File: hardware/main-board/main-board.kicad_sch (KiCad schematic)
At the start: 97 parts, among them J1 BOOT, J10 8P8CDouble, J11 Qwiic, J12 Qwiic, J13 Qwiic, J14 Micro_SD_Card_Det, J15 Interrupts1, J16 Interrupts2, J2 USB Header, J3 JTAG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

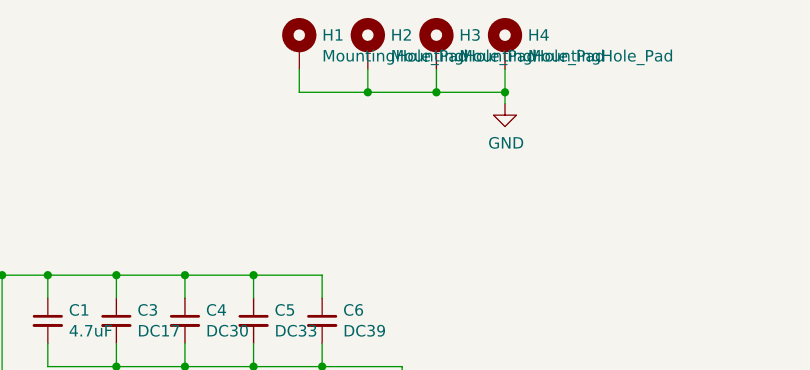
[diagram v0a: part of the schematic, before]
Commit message: Convert all other mounting holes to non-pad variety.
Reroute a few traces to be shorter.
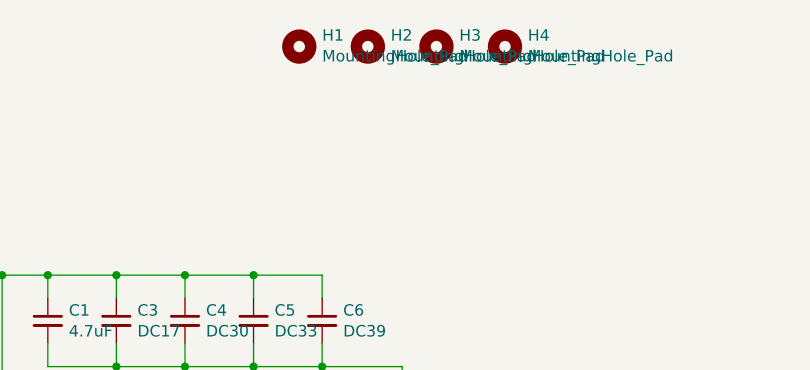
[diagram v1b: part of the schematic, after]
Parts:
- H1, H2, H3, H4: footprint Mounting_Holes:MountingHole_3.2mm_M3_Pad_Via -> MountingHole:MountingHole_3.2mm_M3; symbol Mechanical:MountingHole_Pad -> Mechanical:MountingHole
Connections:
- net GND: no longer H1.1, H2.1, H3.1, H4.1
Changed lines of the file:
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@@
   (junction (at 370.84 76.2) (diameter 0) (color 0 0 0 0)
   )
-  (junction (at 406.4 31.75) (diameter 0) (color 0 0 0 0)
-  )
   (junction (at 425.45 186.69) (diameter 0) (color 0 0 0 0)
   )
@@
   (junction (at 186.69 99.06) (diameter 0) (color 0 0 0 0)
   )
-  (junction (at 414.02 31.75) (diameter 0) (color 0 0 0 0)
-  )
   (junction (at 181.61 317.5) (diameter 0) (color 0 0 0 0)
   )
@@
   (junction (at 49.53 365.76) (diameter 0) (color 0 0 0 0)
   )
-  (junction (at 421.64 31.75) (diameter 0) (color 0 0 0 0)
-  )
   (no_connect (at 334.01 86.36))
   (no_connect (at 270.51 160.02))
@@
     (stroke (width 0) (type default) (color 0 0 0 0))
   )
-  (wire (pts (xy 414.02 29.21) (xy 414.02 31.75))
-    (stroke (width 0) (type default) (color 0 0 0 0))
-  )
   (wire (pts (xy 237.49 121.92) (xy 237.49 123.19))
     (stroke (width 0) (type default) (color 0 0 0 0))
@@
     (stroke (width 0) (type default) (color 0 0 0 0))
   )
-  (wire (pts (xy 421.64 31.75) (xy 421.64 29.21))
-    (stroke (width 0) (type default) (color 0 0 0 0))
-  )
   (wire (pts (xy 361.95 95.25) (xy 361.95 92.71))
     (stroke (width 0) (type default) (color 0 0 0 0))
@@
     (stroke (width 0) (type default) (color 0 0 0 0))
   )
-  (wire (pts (xy 398.78 31.75) (xy 406.4 31.75))
-    (stroke (width 0) (type default) (color 0 0 0 0))
-  )
   (wire (pts (xy 52.07 295.91) (xy 40.64 295.91))
     (stroke (width 0) (type default) (color 0 0 0 0))
@@
     (stroke (width 0) (type default) (color 0 0 0 0))
   )
-  (wire (pts (xy 421.64 33.02) (xy 421.64 31.75))
-    (stroke (width 0) (type default) (color 0 0 0 0))
-  )
   (wire (pts (xy 288.29 359.41) (xy 293.37 359.41))
     (stroke (width 0) (type default) (color 0 0 0 0))
@@
     (stroke (width 0) (type default) (color 0 0 0 0))
   )
-  (wire (pts (xy 406.4 29.21) (xy 406.4 31.75))
-    (stroke (width 0) (type default) (color 0 0 0 0))
-  )
   (wire (pts (xy 290.83 356.87) (xy 290.83 367.03))
     (stroke (width 0) (type default) (color 0 0 0 0))
@@
     (stroke (width 0) (type default) (color 0 0 0 0))
   )
-  (wire (pts (xy 406.4 31.75) (xy 414.02 31.75))
-    (stroke (width 0) (type default) (color 0 0 0 0))
-  )
   (wire (pts (xy 248.92 321.31) (xy 248.92 318.77))
     (stroke (width 0) (type default) (color 0 0 0 0))
@@
     (stroke (width 0) (type default) (color 0 0 0 0))
   )
-  (wire (pts (xy 398.78 29.21) (xy 398.78 31.75))
-    (stroke (width 0) (type default) (color 0 0 0 0))
-  )
   (wire (pts (xy 243.84 387.35) (xy 246.38 387.35))
     (stroke (width 0) (type default) (color 0 0 0 0))
@@
     (stroke (width 0) (type default) (color 0 0 0 0))
   )
-  (wire (pts (xy 414.02 31.75) (xy 421.64 31.75))
-    (stroke (width 0) (type default) (color 0 0 0 0))
-  )
   (wire (pts (xy 487.68 104.14) (xy 487.68 107.95))
     (stroke (width 0) (type default) (color 0 0 0 0))
@@
     (pin "1")
   )
-  (symbol (lib_id "Mechanical:MountingHole_Pad") (at 398.78 26.67 0) (unit 1)
+  (symbol (lib_id "Mechanical:MountingHole") (at 398.78 26.67 0) (unit 1)
     (in_bom yes) (on_board yes)
     (property "Reference" "H1" (id 0) (at 401.32 25.4254 0)
@@
       (effects (font (size 1.27 1.27)) (justify left))
     )
-    (property "Footprint" "Mounting_Holes:MountingHole_3.2mm_M3_Pad_Via" (id 2) (at 398.78 26.67 0)
+    (property "Footprint" "MountingHole:MountingHole_3.2mm_M3" (id 2) (at 398.78 26.67 0)
       (effects (font (size 1.27 1.27)) hide)
     )
@@
       (effects (font (size 1.27 1.27)) hide)
     )
-    (pin "1")
   )
-  (symbol (lib_id "Mechanical:MountingHole_Pad") (at 406.4 26.67 0) (unit 1)
+  (symbol (lib_id "Mechanical:MountingHole") (at 406.4 26.67 0) (unit 1)
     (in_bom yes) (on_board yes)
     (property "Reference" "H2" (id 0) (at 408.94 25.4254 0)
@@
       (effects (font (size 1.27 1.27)) (justify left))
     )
-    (property "Footprint" "Mounting_Holes:MountingHole_3.2mm_M3_Pad_Via" (id 2) (at 406.4 26.67 0)
+    (property "Footprint" "MountingHole:MountingHole_3.2mm_M3" (id 2) (at 406.4 26.67 0)
       (effects (font (size 1.27 1.27)) hide)
     )
@@
       (effects (font (size 1.27 1.27)) hide)
     )
-    (pin "1")
   )
-  (symbol (lib_id "Mechanical:MountingHole_Pad") (at 414.02 26.67 0) (unit 1)
+  (symbol (lib_id "Mechanical:MountingHole") (at 414.02 26.67 0) (unit 1)
     (in_bom yes) (on_board yes)
     (property "Reference" "H3" (id 0) (at 416.56 25.4254 0)
@@
       (effects (font (size 1.27 1.27)) (justify left))
     )
-    (property "Footprint" "Mounting_Holes:MountingHole_3.2mm_M3_Pad_Via" (id 2) (at 414.02 26.67 0)
+    (property "Footprint" "MountingHole:MountingHole_3.2mm_M3" (id 2) (at 414.02 26.67 0)
       (effects (font (size 1.27 1.27)) hide)
     )
@@
       (effects (font (size 1.27 1.27)) hide)
     )
-    (pin "1")
   )
-  (symbol (lib_id "Mechanical:MountingHole_Pad") (at 421.64 26.67 0) (unit 1)
+  (symbol (lib_id "Mechanical:MountingHole") (at 421.64 26.67 0) (unit 1)
     (in_bom yes) (on_board yes)
     (property "Reference" "H4" (id 0) (at 424.18 25.4254 0)
@@
       (effects (font (size 1.27 1.27)) (justify left))
     )
-    (property "Footprint" "Mounting_Holes:MountingHole_3.2mm_M3_Pad_Via" (id 2) (at 421.64 26.67 0)
+    (property "Footprint" "MountingHole:MountingHole_3.2mm_M3" (id 2) (at 421.64 26.67 0)
       (effects (font (size 1.27 1.27)) hide)
     )
@@
       (effects (font (size 1.27 1.27)) hide)
     )
-    (pin "1")
-  )
-  (symbol (lib_id "power:GND") (at 421.64 33.02 0) (unit 1)
-    (in_bom yes) (on_board yes)
-    (property "Reference" "#PWR0114" (id 0) (at 421.64 39.37 0)
-      (effects (font (size 1.27 1.27)) hide)
-    )
-    (property "Value" "GND" (id 1) (at 421.767 37.4142 0))
-    (property "Footprint" "" (id 2) (at 421.64 33.02 0)
-      (effects (font (size 1.27 1.27)) hide)
-    )
-    (property "Datasheet" "" (id 3) (at 421.64 33.02 0)
-      (effects (font (size 1.27 1.27)) hide)
-    )
-    (pin "1")
   )
   (symbol (lib_id "Connector:Conn_01x04_Female") (at 450.85 288.29 180) (unit 1)
@@
       (reference "#PWR0113") (unit 1) (value "GND") (footprint "")
     )
-    (path "/00000000-0000-0000-0000-0000600a4486"
-      (reference "#PWR0114") (unit 1) (value "GND") (footprint "")
-    )
     (path "/00000000-0000-0000-0000-000060a745cc"
       (reference "#PWR0115") (unit 1) (value "GND") (footprint "")
@@
     )
     (path "/00000000-0000-0000-0000-0000600a2ea9"
-      (reference "H1") (unit 1) (value "MountingHole_Pad") (footprint "Mounting_Holes:MountingHole_3.2mm_M3_Pad_Via")
+      (reference "H1") (unit 1) (value "MountingHole_Pad") (footprint "MountingHole:MountingHole_3.2mm_M3")
     )
     (path "/00000000-0000-0000-0000-0000600a385e"
-      (reference "H2") (unit 1) (value "MountingHole_Pad") (footprint "Mounting_Holes:MountingHole_3.2mm_M3_Pad_Via")
+      (reference "H2") (unit 1) (value "MountingHole_Pad") (footprint "MountingHole:MountingHole_3.2mm_M3")
     )
     (path "/00000000-0000-0000-0000-0000600a3c05"
-      (reference "H3") (unit 1) (value "MountingHole_Pad") (footprint "Mounting_Holes:MountingHole_3.2mm_M3_Pad_Via")
+      (reference "H3") (unit 1) (value "MountingHole_Pad") (footprint "MountingHole:MountingHole_3.2mm_M3")
     )
     (path "/00000000-0000-0000-0000-0000600a3fdf"
-      (reference "H4") (unit 1) (value "MountingHole_Pad") (footprint "Mounting_Holes:MountingHole_3.2mm_M3_Pad_Via")
+      (reference "H4") (unit 1) (value "MountingHole_Pad") (footprint "MountingHole:MountingHole_3.2mm_M3")
     )
     (path "/00000000-0000-0000-0000-000060c0234f"
